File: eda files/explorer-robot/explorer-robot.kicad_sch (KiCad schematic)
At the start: 0 parts

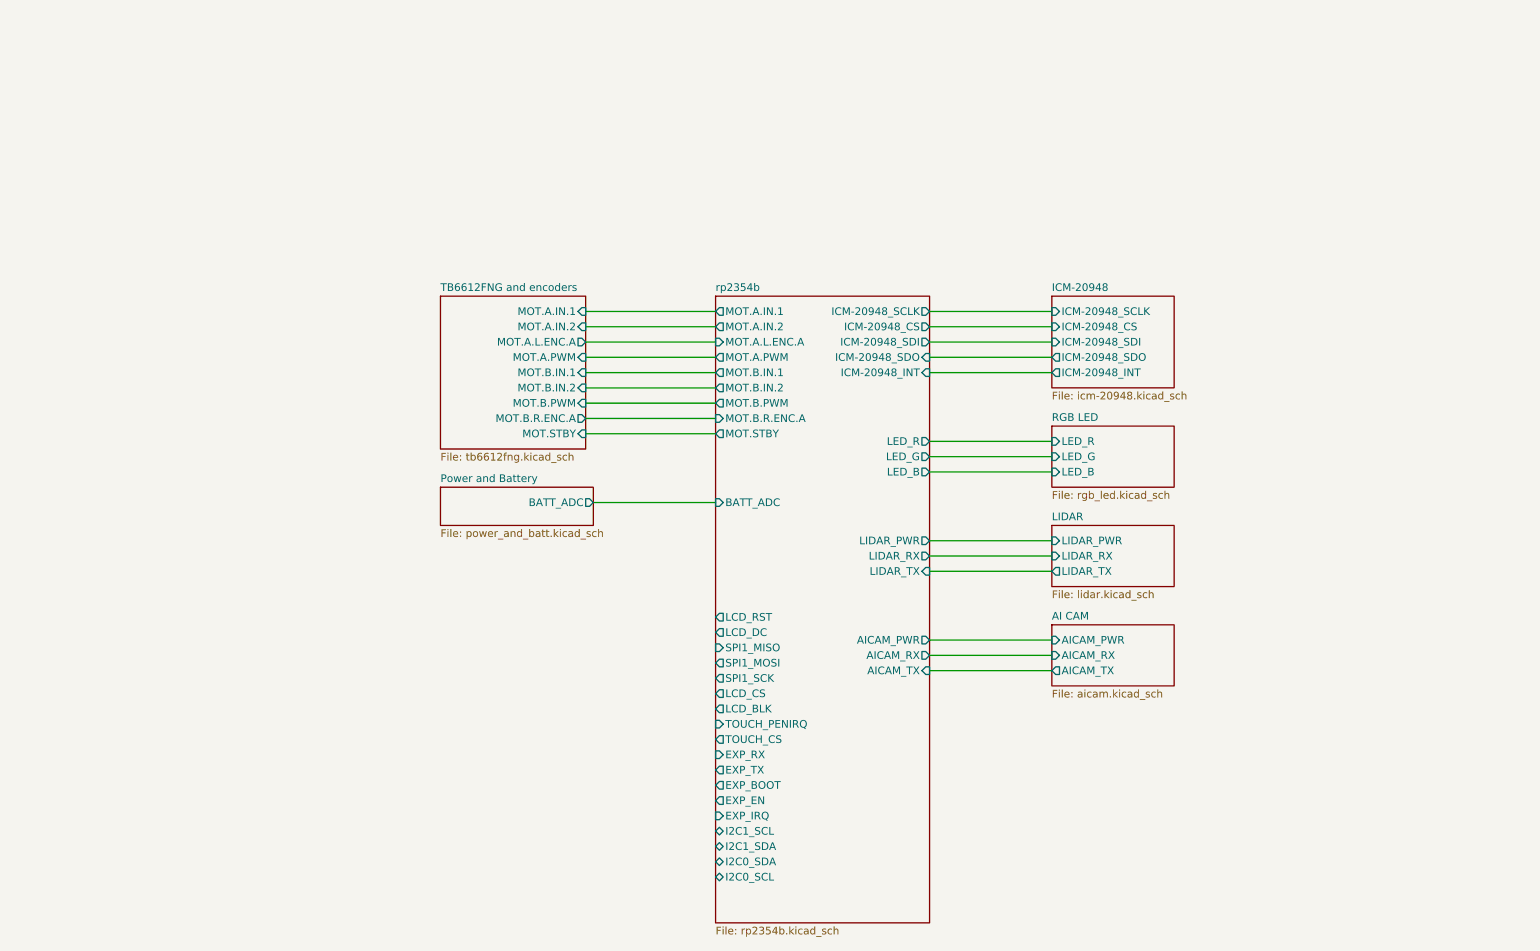
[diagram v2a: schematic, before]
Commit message: Add expansion connector sheet and hierarchical wiring
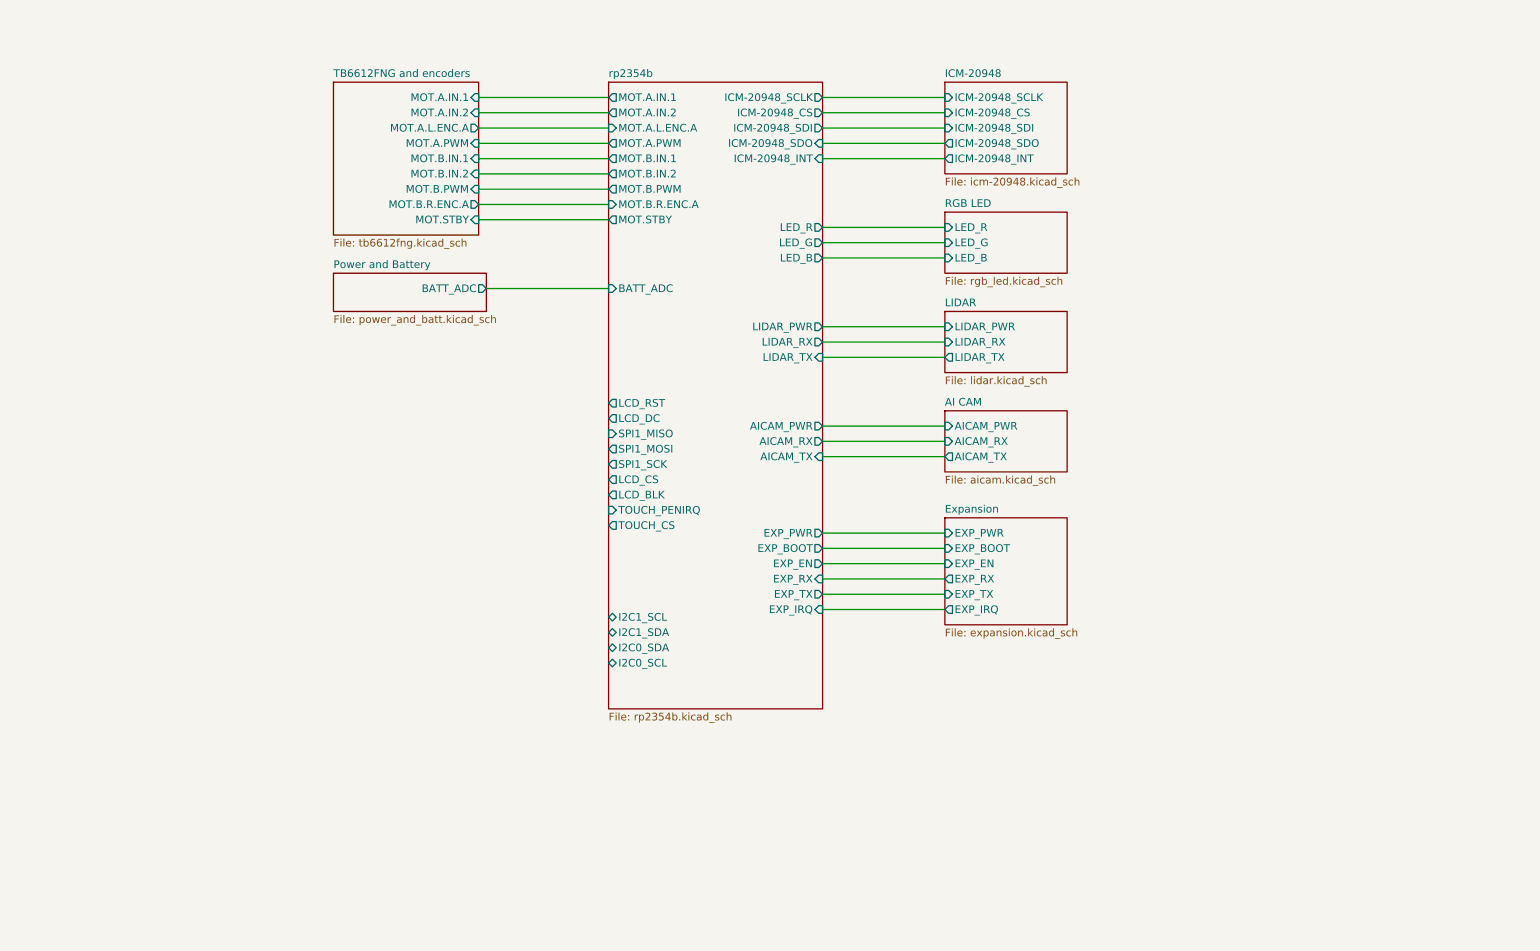
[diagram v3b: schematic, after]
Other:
- added sheet Expansion (expansion.kicad_sch)
- sheet rp2354b ports: added EXP_PWR; removed none

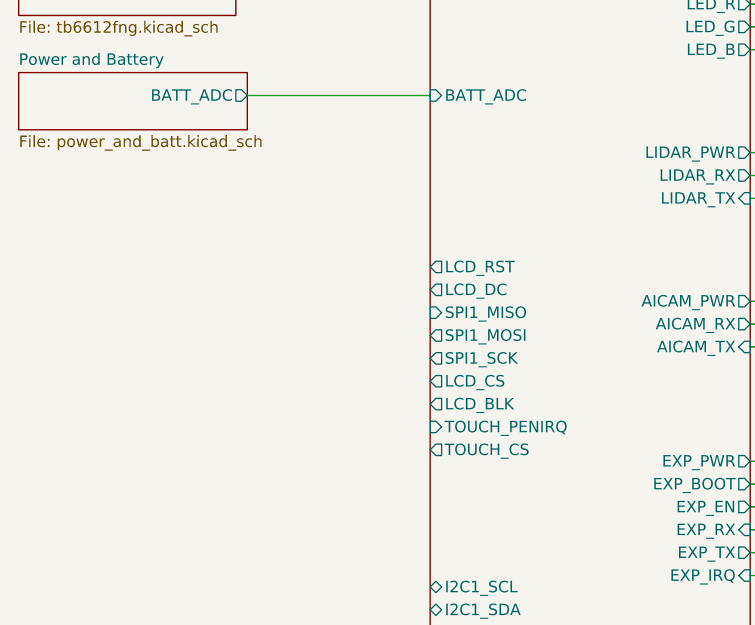
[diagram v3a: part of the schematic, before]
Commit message: Add switched 5 V panel branch with series resistors
The panel harness splits into PANEL.BUS (5 V, GND, shared SPI1 lines)
and
PANEL.CTRL (control lines) so a mis-plugged cable cannot short 5 V onto
a
3.3 V GPIO. A TPS22917 load switch on GPIO0 gates the panel's 5 V, and
series resistors (33 Ω on the 64 MHz SPI lines, 100 Ω on the slow
control
lines, 1 kΩ on TOUCH_PENIRQ) bound fault current and damp the bus.

GPIO0 leaves the spare pool; GPIO1–3 and GPIO31 remain spare. See
ADR-0024.
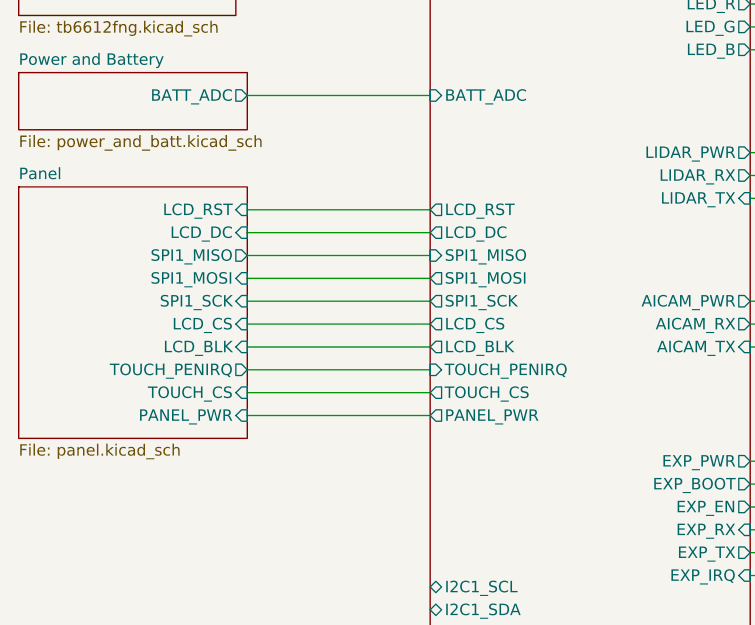
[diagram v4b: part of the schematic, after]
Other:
- added sheet Panel (panel.kicad_sch)
- sheet rp2354b ports: added PANEL_PWR; removed none

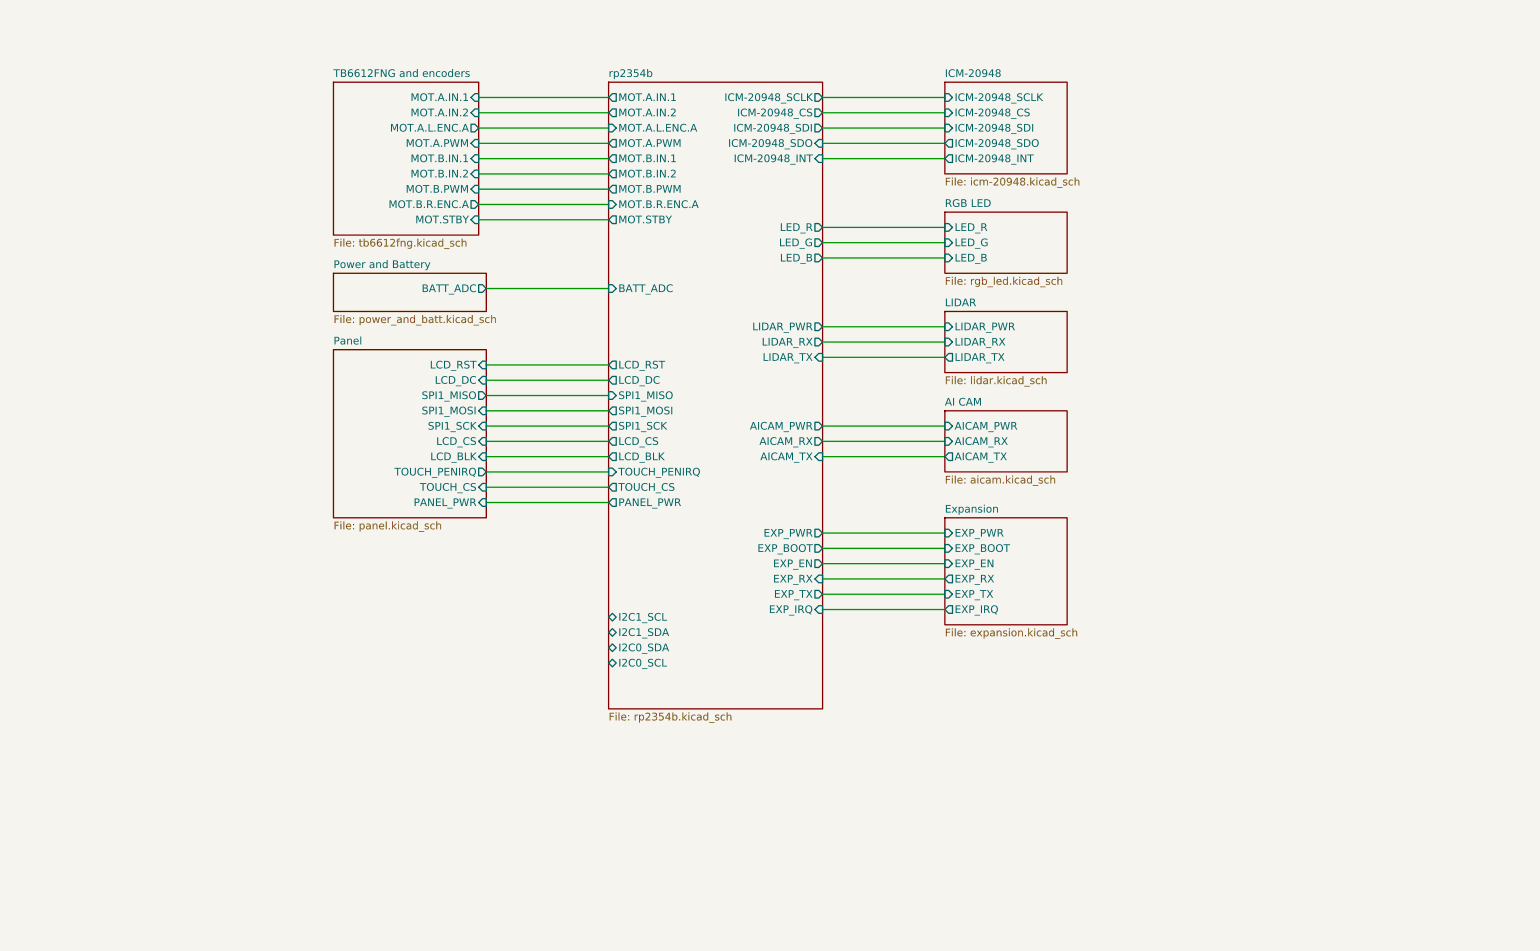
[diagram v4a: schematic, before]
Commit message: Add rear rangefinder to schematic and docs
Document the rear VL53L0X module as a second floor-drop sensor on
I2C1. Add ADR-0026 covering the two unswitched 3.3 V connectors, their
XSHUT/INT GPIO assignments (1-3, 31), pull-ups and series resistors,
and the new rangefinders schematic sheet. Amend ADR-0021, ADR-0022 and
ADR-0024 to note the GPIOs are no longer spare, and update CONTEXT,
README and firmware docs to describe the front/rear pair.
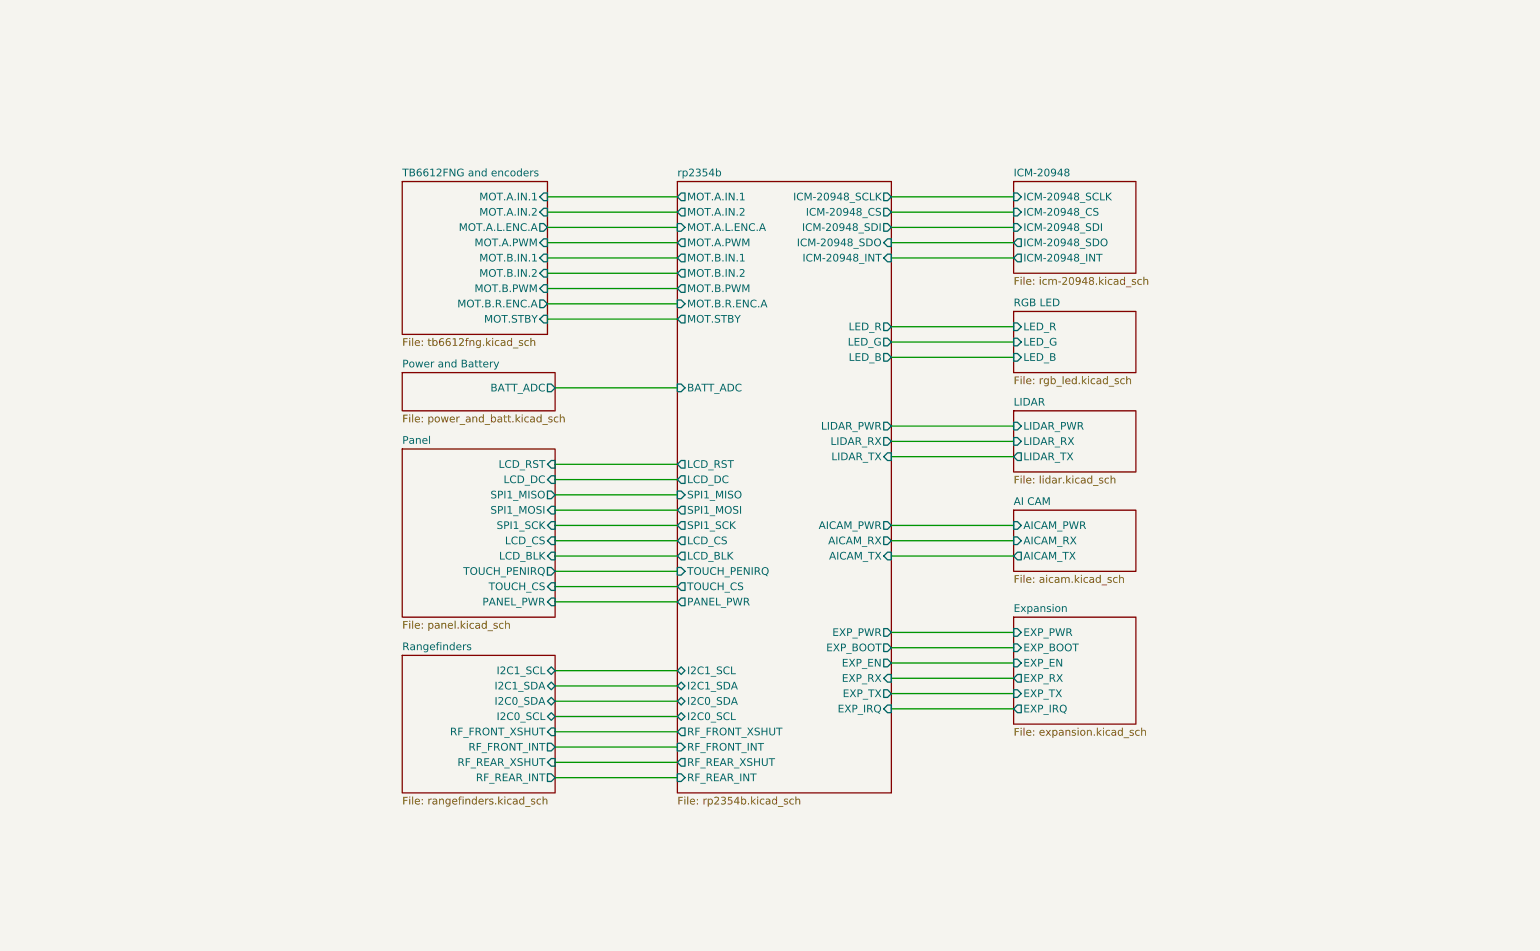
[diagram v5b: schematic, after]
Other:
- added sheet Rangefinders (rangefinders.kicad_sch)
- sheet rp2354b ports: added RF_FRONT_INT, RF_FRONT_XSHUT, RF_REAR_INT, RF_REAR_XSHUT; removed none

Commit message: Update AI camera branch to 5V and document schematic
- ADR-0027 supersedes ADR-0025: AI camera input is 5V, not 3.3V
- Move U9 VIN and C55 back to +5V in aicam.kicad_sch
- Update CONTEXT.md branch descriptions and ADR cross-references
- Record ICM-20948 placement status and corrected battery divider ratio
- Adjust battery_charge_read for 33k/10k divider (0.2326 ratio)
- Enable sheet component classes; refresh netlist and PCB footprints
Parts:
- added H1, H2, H3, H4: MountingHole_Pad, MountingHole:MountingHole_3.2mm_M3_Pad_Via, symbol Mechanical:MountingHole_Pad
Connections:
- new net GND: H1.1, H2.1, H3.1, H4.1
